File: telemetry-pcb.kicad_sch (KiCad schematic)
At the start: 25 parts

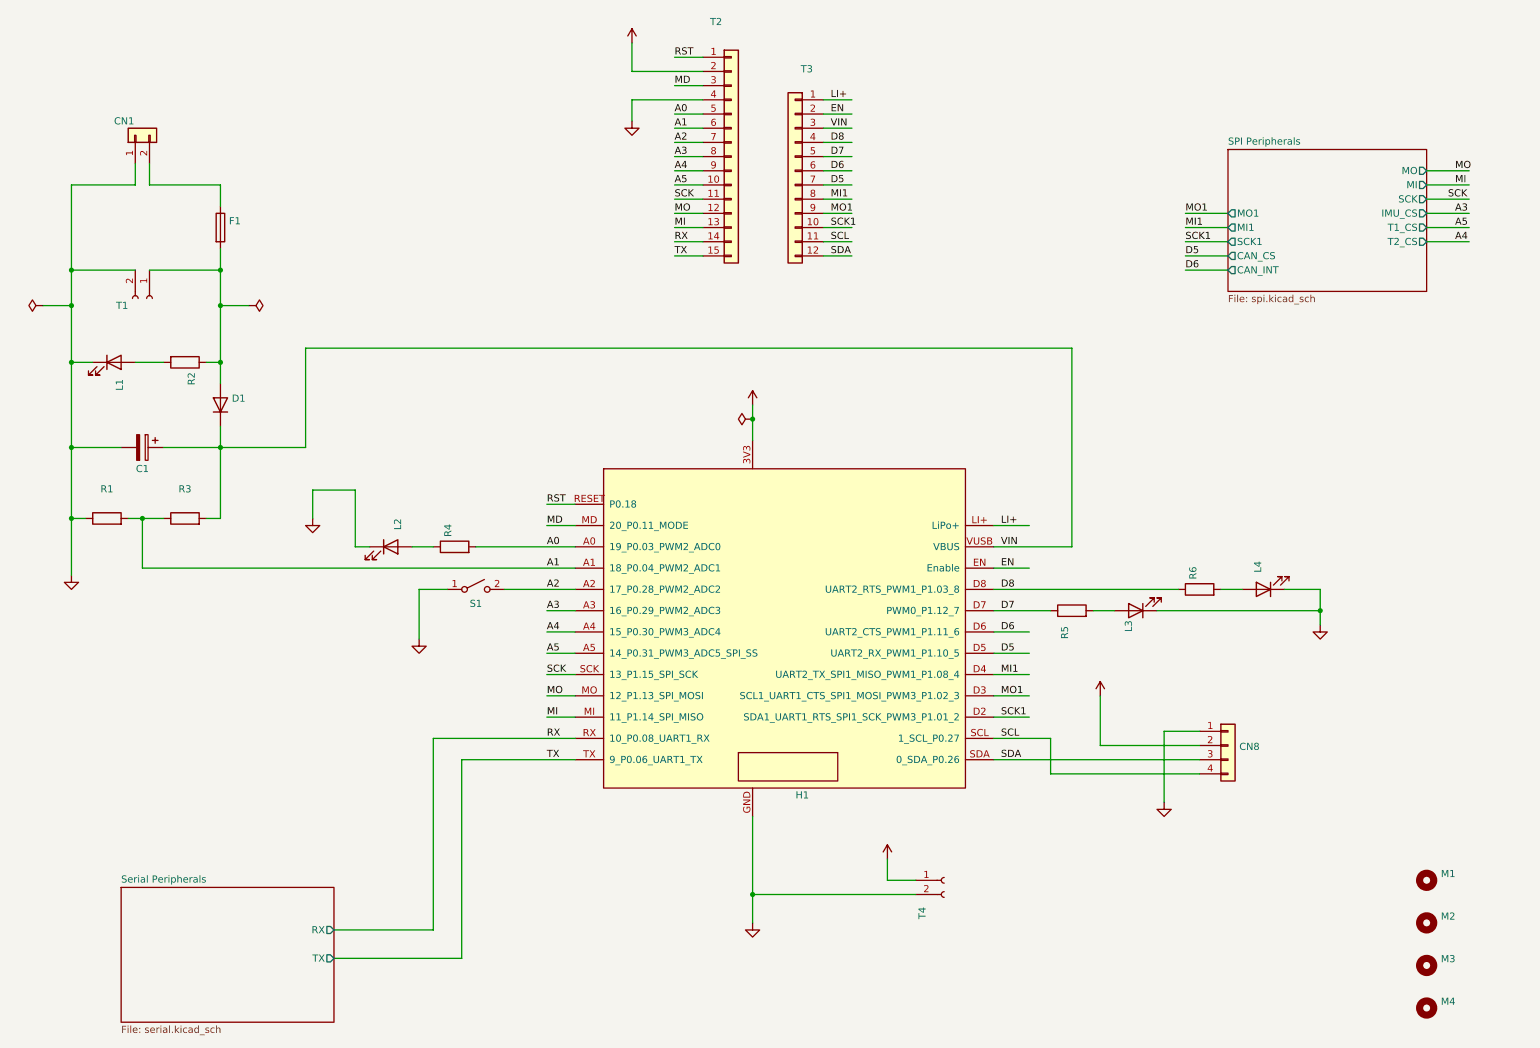
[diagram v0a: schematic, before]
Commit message: fixed power flag in schematic causing error
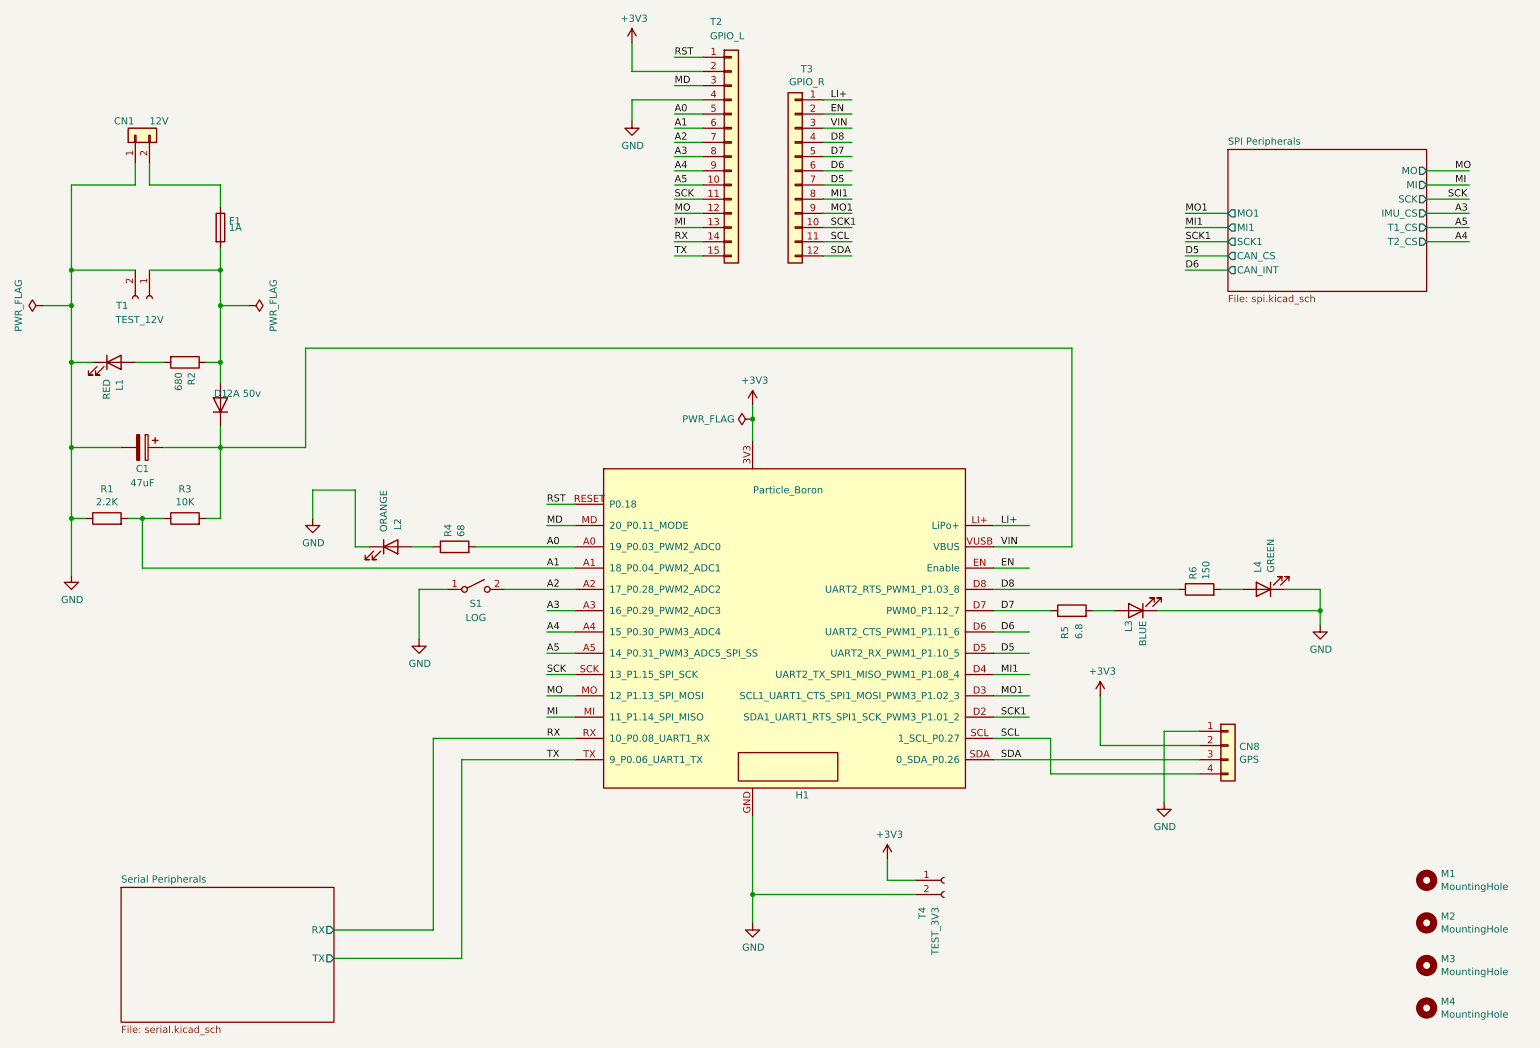
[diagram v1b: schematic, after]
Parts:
- C1: value (none) -> 47uF; footprint (none) -> Capacitor_SMD:CP_Elec_6.3x5.4
- CN1: value (none) -> 12V; footprint (none) -> telemetry-pcb:molex_sl_1x02_horizontal
- CN8: value (none) -> GPS; footprint (none) -> Connector_JST:JST_GH_SM04B-GHS-TB_1x04-1MP_P1.25mm_Horizontal
- D1: value (none) -> 2A 50v; footprint (none) -> Diode_SMD:D_SMA
- F1: value (none) -> 1A; footprint (none) -> telemetry-pcb:0154001.DRL
- H1: value (none) -> Particle_Boron; footprint (none) -> telemetry-pcb:Particle_boron
- L1: value (none) -> RED; footprint (none) -> LED_SMD:LED_0805_2012Metric
- L2: value (none) -> ORANGE; footprint (none) -> LED_SMD:LED_0805_2012Metric
- L3: value (none) -> BLUE; footprint (none) -> LED_SMD:LED_0805_2012Metric
- L4: value (none) -> GREEN; footprint (none) -> LED_SMD:LED_0805_2012Metric
- M1, M2, M3, M4: value (none) -> MountingHole; footprint (none) -> MountingHole:MountingHole_3.2mm_M3
- R1: value (none) -> 2.2K; footprint (none) -> Resistor_SMD:R_0805_2012Metric
- R2: value (none) -> 680; footprint (none) -> Resistor_SMD:R_0805_2012Metric
- R3: value (none) -> 10K; footprint (none) -> Resistor_SMD:R_0805_2012Metric
- R4: value (none) -> 68; footprint (none) -> Resistor_SMD:R_0805_2012Metric
- R5: value (none) -> 6.8; footprint (none) -> Resistor_SMD:R_0805_2012Metric
- R6: value (none) -> 150; footprint (none) -> Resistor_SMD:R_0805_2012Metric
- S1: value (none) -> LOG; footprint (none) -> Button_Switch_THT:SW_PUSH_6mm_H13mm
- T1: value (none) -> TEST_12V; footprint (none) -> TestPoint:TestPoint_2Pads_Pitch2.54mm_Drill0.8mm
- T2: value (none) -> GPIO_L; footprint (none) -> telemetry-pcb:Boron_Pins_L
- T3: value (none) -> GPIO_R; footprint (none) -> telemetry-pcb:Boron_Pins_R
- T4: value (none) -> TEST_3V3; footprint (none) -> TestPoint:TestPoint_2Pads_Pitch2.54mm_Drill0.8mm

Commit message: 3.0 Preliminary Changes
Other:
- moved on the sheet: L2, R4

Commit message: 3.0 Preliminary Changes
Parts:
- removed L2: ORANGE, LED_SMD:LED_0805_2012Metric, symbol Device:LED
- removed R4: 68, Resistor_SMD:R_0805_2012Metric, symbol Device:R
- added S2: SELECT, Button_Switch_THT:SW_PUSH_6mm_H13mm, symbol Switch:SW_SPST
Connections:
- net A0: now also S2.2 (B)
- net GND: now also S2.1 (A)
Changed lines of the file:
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@@
 	(wire
 		(pts
-			(xy 95.25 102.87) (xy 111.76 102.87)
+			(xy 101.6 102.87) (xy 111.76 102.87)
 		)
 		(stroke
@@
 	(wire
 		(pts
-			(xy 95.25 92.71) (xy 95.25 102.87)
-		)
-		(stroke
-			(width 0)
-			(type default)
-		)
-	)
-	(wire
-		(pts
 			(xy 205.74 129.54) (xy 205.74 138.43)
 		)
@@
 	(wire
 		(pts
-			(xy 86.36 92.71) (xy 82.55 92.71)
-		)
-		(stroke
-			(width 0)
-			(type default)
-		)
-	)
-	(wire
-		(pts
 			(xy 21.59 85.09) (xy 30.48 85.09)
 		)
@@
 	(wire
 		(pts
-			(xy 21.59 38.1) (xy 33.02 38.1)
+			(xy 101.6 87.63) (xy 99.06 87.63)
 		)
 		(stroke
@@
 	(wire
 		(pts
-			(xy 134.62 30.48) (xy 129.54 30.48)
+			(xy 21.59 38.1) (xy 33.02 38.1)
 		)
 		(stroke
@@
 	(wire
 		(pts
-			(xy 69.85 92.71) (xy 74.93 92.71)
+			(xy 134.62 30.48) (xy 129.54 30.48)
 		)
 		(stroke
@@
 	(wire
 		(pts
+			(xy 88.9 87.63) (xy 83.82 87.63)
+		)
+		(stroke
+			(width 0)
+			(type default)
+		)
+	)
+	(wire
+		(pts
 			(xy 134.62 27.94) (xy 129.54 27.94)
 		)
@@
 	(wire
 		(pts
-			(xy 69.85 92.71) (xy 69.85 97.79)
-		)
-		(stroke
-			(width 0)
-			(type default)
-		)
-	)
-	(wire
-		(pts
 			(xy 99.06 110.49) (xy 111.76 110.49)
 		)
@@
 	(wire
 		(pts
-			(xy 93.98 92.71) (xy 95.25 92.71)
-		)
-		(stroke
-			(width 0)
-			(type default)
-		)
-	)
-	(wire
-		(pts
 			(xy 186.69 99.06) (xy 193.04 99.06)
 		)
@@
 	(wire
 		(pts
+			(xy 101.6 87.63) (xy 101.6 102.87)
+		)
+		(stroke
+			(width 0)
+			(type default)
+		)
+	)
+	(wire
+		(pts
 			(xy 134.62 20.32) (xy 129.54 20.32)
 		)
@@
 	(wire
 		(pts
+			(xy 83.82 87.63) (xy 83.82 96.52)
+		)
+		(stroke
+			(width 0)
+			(type default)
+		)
+	)
+	(wire
+		(pts
 			(xy 21.59 53.34) (xy 33.02 53.34)
 		)
@@
 	)
 	(symbol
-		(lib_id "Device:LED")
-		(at 78.74 92.71 0)
-		(unit 1)
-		(exclude_from_sim no)
-		(in_bom yes)
-		(on_board yes)
-		(dnp no)
-		(property "Reference" "L2"
-			(at 80.01 87.63 90)
-			(effects
-				(font
-					(size 1.27 1.27)
-				)
-				(justify right)
-			)
-		)
-		(property "Value" "ORANGE"
-			(at 77.47 82.55 90)
-			(effects
-				(font
-					(size 1.27 1.27)
-				)
-				(justify right)
-			)
-		)
-		(property "Footprint" "LED_SMD:LED_0805_2012Metric"
-			(at 78.74 92.71 0)
-			(effects
-				(font
-					(size 1.27 1.27)
-				)
-				(hide yes)
-			)
-		)
-		(property "Datasheet" "~"
-			(at 78.74 92.71 0)
-			(effects
-				(font
-					(size 1.27 1.27)
-				)
-				(hide yes)
-			)
-		)
-		(property "Description" ""
-			(at 78.74 92.71 0)
-			(effects
-				(font
-					(size 1.27 1.27)
-				)
-			)
-		)
-		(pin "1"
-		)
-		(pin "2"
-		)
-		(instances
-			(project "telemetry-pcb"
-				(path "/871fe08d-2afd-493a-a8ef-c8aa2cbbb7b9"
-					(reference "L2")
-					(unit 1)
-				)
-			)
-		)
-	)
-	(symbol
 		(lib_id "Device:R")
 		(at 223.52 110.49 90)
@@
 	)
 	(symbol
-		(lib_id "Device:R")
-		(at 90.17 92.71 90)
-		(unit 1)
-		(exclude_from_sim no)
-		(in_bom yes)
-		(on_board yes)
-		(dnp no)
-		(property "Reference" "R4"
-			(at 89.0016 90.932 0)
-			(effects
-				(font
-					(size 1.27 1.27)
-				)
-				(justify left)
-			)
-		)
-		(property "Value" "68"
-			(at 91.313 90.932 0)
-			(effects
-				(font
-					(size 1.27 1.27)
-				)
-				(justify left)
-			)
-		)
-		(property "Footprint" "Resistor_SMD:R_0805_2012Metric"
-			(at 90.17 94.488 90)
-			(effects
-				(font
-					(size 1.27 1.27)
-				)
-				(hide yes)
-			)
-		)
-		(property "Datasheet" "~"
-			(at 90.17 92.71 0)
-			(effects
-				(font
-					(size 1.27 1.27)
-				)
-				(hide yes)
-			)
-		)
-		(property "Description" ""
-			(at 90.17 92.71 0)
-			(effects
-				(font
-					(size 1.27 1.27)
-				)
-			)
-		)
-		(pin "1"
-		)
-		(pin "2"
-		)
-		(instances
-			(project "telemetry-pcb"
-				(path "/871fe08d-2afd-493a-a8ef-c8aa2cbbb7b9"
-					(reference "R4")
-					(unit 1)
-				)
-			)
-		)
-	)
-	(symbol
 		(lib_id "power:+3V3")
 		(at 205.74 129.54 0)
@@
 	)
 	(symbol
-		(lib_id "power:GND")
-		(at 69.85 97.79 0)
-		(unit 1)
-		(exclude_from_sim no)
-		(in_bom yes)
-		(on_board yes)
-		(dnp no)
-		(property "Reference" "#PWR02"
-			(at 69.85 104.14 0)
-			(effects
-				(font
-					(size 1.27 1.27)
-				)
-				(hide yes)
-			)
-		)
-		(property "Value" "GND"
-			(at 69.977 102.1842 0)
-			(effects
-				(font
-					(size 1.27 1.27)
-				)
-			)
-		)
-		(property "Footprint" ""
-			(at 69.85 97.79 0)
-			(effects
-				(font
-					(size 1.27 1.27)
-				)
-				(hide yes)
-			)
-		)
-		(property "Datasheet" ""
-			(at 69.85 97.79 0)
-			(effects
-				(font
-					(size 1.27 1.27)
-				)
-				(hide yes)
-			)
-		)
-		(property "Description" ""
-			(at 69.85 97.79 0)
-			(effects
-				(font
-					(size 1.27 1.27)
-				)
-			)
-		)
-		(pin "1"
-		)
-		(instances
-			(project "telemetry-pcb"
-				(path "/871fe08d-2afd-493a-a8ef-c8aa2cbbb7b9"
-					(reference "#PWR02")
-					(unit 1)
-				)
-			)
-		)
-	)
-	(symbol
 		(lib_id "Connector:Conn_01x02_Female")
 		(at 177.8 162.56 0)
@@
 					(unit 1)
 				)
+			)
+		)
+	)
+	(symbol
+		(lib_id "Switch:SW_SPST")
+		(at 93.98 87.63 0)
+		(unit 1)
+		(exclude_from_sim no)
+		(in_bom yes)
+		(on_board yes)
+		(dnp no)
+		(property "Reference" "S2"
+			(at 93.98 90.17 0)
+			(effects
+				(font
+					(size 1.27 1.27)
+				)
+			)
+		)
+		(property "Value" "SELECT"
+			(at 93.98 92.71 0)
+			(effects
+				(font
+					(size 1.27 1.27)
+				)
+			)
+		)
+		(property "Footprint" "Button_Switch_THT:SW_PUSH_6mm_H13mm"
+			(at 93.98 87.63 0)
+			(effects
+				(font
+					(size 1.27 1.27)
+				)
+				(hide yes)
+			)
+		)
+		(property "Datasheet" "~"
+			(at 93.98 87.63 0)
+			(effects
+				(font
+					(size 1.27 1.27)
+				)
+				(hide yes)
+			)
+		)
+		(property "Description" ""
+			(at 93.98 87.63 0)
+			(effects
+				(font
+					(size 1.27 1.27)
+				)
+			)
+		)
+		(pin "1"
+		)
+		(pin "2"
+		)
+		(instances
+			(project "telemetry-pcb"
+				(path "/871fe08d-2afd-493a-a8ef-c8aa2cbbb7b9"
+					(reference "S2")
+					(unit 1)
+				)
+			)
+		)
+	)
+	(symbol
+		(lib_id "power:GND")
+		(at 83.82 96.52 0)
+		(unit 1)
+		(exclude_from_sim no)
+		(in_bom yes)
+		(on_board yes)
+		(dnp no)
+		(property "Reference" "#PWR02"
+			(at 83.82 102.87 0)
+			(effects
+				(font
+					(size 1.27 1.27)
+				)
+				(hide yes)
+			)
+		)
+		(property "Value" "GND"
+			(at 83.947 100.9142 0)
+			(effects
+				(font
+					(size 1.27 1.27)
+				)
+			)
+		)
+		(property "Footprint" ""
+			(at 83.82 96.52 0)
+			(effects
+				(font
+					(size 1.27 1.27)
+				)
+				(hide yes)
+			)
+		)
+		(property "Datasheet" ""
+			(at 83.82 96.52 0)
+			(effects
+				(font
+					(size 1.27 1.27)
+				)
+				(hide yes)
+			)
+		)
+		(property "Description" ""
+			(at 83.82 96.52 0)
+			(effects
+				(font
+					(size 1.27 1.27)
+				)
+			)
+		)
+		(pin "1"
+		)
+		(instances
+			(project "telemetry-pcb"
+				(path "/871fe08d-2afd-493a-a8ef-c8aa2cbbb7b9"
+					(reference "#PWR02")
+					(unit 1)
+				)

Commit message: backup
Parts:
- removed R1: 2.2K, Resistor_SMD:R_0805_2012Metric, symbol Device:R
- removed R3: 10K, Resistor_SMD:R_0805_2012Metric, symbol Device:R
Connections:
- net A1: no longer H1.A1 (18_P0.04_PWM2_ADC1)
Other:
- moved on the sheet: CN8
